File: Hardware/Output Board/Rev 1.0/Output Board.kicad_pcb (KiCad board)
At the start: 2 copper layers, 100 x 100 mm, 13 parts, among them J1 6502 Bus, J3 Conn_02x08_Odd_Even, U2 74HC138

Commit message: Working on Output Board
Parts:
- added C1: 100nF, Capacitor_SMD:C_0805_2012Metric, F.Cu at (109.5, 99.0)
- added C10: 100nF, Capacitor_SMD:C_0805_2012Metric, F.Cu at (130.8, 101.2)
- added C11: 4.7uF, Capacitor_SMD:C_0805_2012Metric, F.Cu at (130.8, 104.2)
- added C12: 4.7uF, Capacitor_SMD:C_0805_2012Metric, F.Cu at (130.8, 107.2)
- added C13: 100nF, Capacitor_SMD:C_0805_2012Metric, F.Cu at (99.6, 67.5)
- added C14: 100nF, Capacitor_SMD:C_0805_2012Metric, F.Cu at (131.8, 86.8)
- added C15: 2.7nF, Capacitor_SMD:C_0805_2012Metric, F.Cu at (111.2, 135.2)
- added C16: 100nF, Capacitor_SMD:C_0805_2012Metric, F.Cu at (105.8, 124.8)
- added C17: 100nF, Capacitor_SMD:C_0805_2012Metric, F.Cu at (157.8, 100.0)
- added C18: 100nF, Capacitor_SMD:C_0805_2012Metric, F.Cu at (162.2, 100.0)
- added C19: 100nF, Capacitor_SMD:C_0805_2012Metric, F.Cu at (157.8, 116.4)
- added C20: 1uF, Capacitor_SMD:C_0805_2012Metric, F.Cu at (115.7, 132.2)
- added C21: 2.7nF, Capacitor_SMD:C_0805_2012Metric, F.Cu at (115.7, 135.2)
- added C22: 2.2uF, Capacitor_SMD:C_0805_2012Metric, F.Cu at (120.2, 120.2)
- added C23: 1uF, Capacitor_SMD:C_0805_2012Metric, F.Cu at (120.2, 123.2)
- added C24: 4.7uF, Capacitor_SMD:C_0805_2012Metric, F.Cu at (120.2, 126.2)
- added C25: 4.7uF, Capacitor_SMD:C_0805_2012Metric, F.Cu at (120.2, 129.2)
- added C26: 10uF, Capacitor_SMD:C_0805_2012Metric, F.Cu at (125.2, 86.6)
- added C27: 10uF, Capacitor_SMD:C_0805_2012Metric, F.Cu at (113.7, 92.5)
- added C28: 10uF, Capacitor_SMD:C_0805_2012Metric, F.Cu at (141.6, 86.2)
- added C29: 10uF, Capacitor_SMD:C_0805_2012Metric, F.Cu at (146.3, 89.9)
- added C30: 100nF, Capacitor_SMD:C_0805_2012Metric, F.Cu at (173.2, 62.2)
- added C31: 100nF, Capacitor_SMD:C_0805_2012Metric, F.Cu at (158.3, 135.2)
- added C32: 100nF, Capacitor_SMD:C_0805_2012Metric, F.Cu at (161.9, 82.3)
- added C33: 100nF, Capacitor_SMD:C_0805_2012Metric, F.Cu at (180.3, 121.5)
- added C5: 100nF, Capacitor_SMD:C_0805_2012Metric, F.Cu at (126.3, 104.2)
- added C6: 100nF, Capacitor_SMD:C_0805_2012Metric, F.Cu at (126.3, 107.2)
- added C7: 4.7uF, Capacitor_SMD:C_0805_2012Metric, F.Cu at (126.3, 110.2)
- added C8: 4.7uF, Capacitor_SMD:C_0805_2012Metric, F.Cu at (126.3, 113.2)
- added C9: 100nF, Capacitor_SMD:C_0805_2012Metric, F.Cu at (126.3, 116.2)
- added J1: PROG, Connector_PinHeader_2.54mm:PinHeader_1x08_P2.54mm_Vertical, F.Cu at (97.7, 81.5)
- added J2: SD CARD, 6502 Parts:10067847-001RLF, F.Cu at (124.1, 55.7)
- added J3: AUDIO L, 6502 Parts:SWITCHCRAFT_PJRAN1X1U02X, F.Cu at (110.0, 145.7)
- added J4: AUDIO R, 6502 Parts:SWITCHCRAFT_PJRAN1X1U02X, F.Cu at (122.2, 145.8)
- added J5: VGA, Connector_Dsub:DSUB-15-HD_Socket_Horizontal_P2.29x1.90mm_EdgePinOffset3.03mm_Housed_MountingHolesOffset4.94mm, F.Cu at (154.6, 143.0)
- added JP1: FLASH EN, Connector_PinHeader_2.54mm:PinHeader_1x02_P2.54mm_Vertical, F.Cu at (98.0, 111.3)
- added JP2: SolderJumper_2_Open, Jumper:SolderJumper-2_P1.3mm_Open_RoundedPad1.0x1.5mm, F.Cu at (152.7, 130.9)
- added JP3: SolderJumper_2_Bridged, Jumper:SolderJumper-2_P1.3mm_Bridged_RoundedPad1.0x1.5mm, F.Cu at (166.8, 124.6)
- added L1: NRS4018T2R2MDGJ, Inductor_SMD:L_Bourns-SRN4018, F.Cu at (113.7, 87.4)
- added R1: 10k, Resistor_SMD:R_0805_2012Metric, F.Cu at (102.5, 87.3)
- added R10: 560, Resistor_SMD:R_0805_2012Metric, F.Cu at (113.4, 125.0)
- added R11: 536, Resistor_SMD:R_0805_2012Metric, F.Cu at (137.2, 122.1)
- added R12: 1070, Resistor_SMD:R_0805_2012Metric, F.Cu at (137.2, 125.0)
- added R13: 47k, Resistor_SMD:R_0805_2012Metric, F.Cu at (93.2, 128.8)
- added R14: 47k, Resistor_SMD:R_0805_2012Metric, F.Cu at (105.7, 127.6)
- added R15: 560, Resistor_SMD:R_0805_2012Metric, F.Cu at (111.1, 129.3)
- added R16: 2150, Resistor_SMD:R_0805_2012Metric, F.Cu at (137.2, 136.8)
- added R17: 4300, Resistor_SMD:R_0805_2012Metric, F.Cu at (141.6, 116.2)
- added R18: 536, Resistor_SMD:R_0805_2012Metric, F.Cu at (141.6, 119.2)
- added R19: 1070, Resistor_SMD:R_0805_2012Metric, F.Cu at (141.6, 122.1)
- added R2: 10k, Resistor_SMD:R_0805_2012Metric, F.Cu at (102.5, 90.2)
- added R20: 47k, Resistor_SMD:R_0805_2012Metric, F.Cu at (117.7, 91.6)
- added R21: 820, Resistor_SMD:R_0805_2012Metric, F.Cu at (141.6, 128.0)
- added R22: 2150, Resistor_SMD:R_0805_2012Metric, F.Cu at (141.6, 130.9)
- added R23: 47k, Resistor_SMD:R_0805_2012Metric, F.Cu at (121.4, 91.6)
- added R24: 820, Resistor_SMD:R_0805_2012Metric, F.Cu at (141.6, 136.8)
- added R25: 4300, Resistor_SMD:R_0805_2012Metric, F.Cu at (146.0, 116.2)
- added R26: 536, Resistor_SMD:R_0805_2012Metric, F.Cu at (146.0, 119.2)
- added R27: 1070, Resistor_SMD:R_0805_2012Metric, F.Cu at (146.0, 122.1)
- added R28: 2150, Resistor_SMD:R_0805_2012Metric, F.Cu at (146.0, 125.0)
- added R29: 4300, Resistor_SMD:R_0805_2012Metric, F.Cu at (146.0, 128.0)
- added R3: 10k, Resistor_SMD:R_0805_2012Metric, F.Cu at (102.5, 93.2)
- added R4: 47k, Resistor_SMD:R_0805_2012Metric, F.Cu at (100.9, 62.3)
- added R5: 47k, Resistor_SMD:R_0805_2012Metric, F.Cu at (95.6, 72.0)
- added R6: 47k, Resistor_SMD:R_0805_2012Metric, F.Cu at (105.7, 57.5)
- added R7: 47k, Resistor_SMD:R_0805_2012Metric, F.Cu at (95.7, 77.1)
- added R8: 47k, Resistor_SMD:R_0805_2012Metric, F.Cu at (105.8, 61.9)
- added R9: 47k, Resistor_SMD:R_0805_2012Metric, F.Cu at (95.3, 67.6)
- added U1: ICE40UP5K-SG48ITR50, Package_DFN_QFN:QFN-48-1EP_7x7mm_P0.5mm_EP5.3x5.3mm, F.Cu at (140.2, 100.1)
- added U10: 74HC138, Package_SO:SOIC-16_3.9x9.9mm_P1.27mm, F.Cu at (160.0, 126.4)
- added U11: 74HC138, Package_SO:SOIC-16_3.9x9.9mm_P1.27mm, F.Cu at (164.0, 74.2)
- added U3: SN74CBTD3861PWR, Package_SO:TSSOP-24_4.4x7.8mm_P0.65mm, F.Cu at (160.0, 110.0)
- added U4: 74CBTLV3126PW, Package_SO:TSSOP-14_4.4x5mm_P0.65mm, F.Cu at (102.2, 73.0)
- added U5: 74LVC4245APW, Package_SO:TSSOP-24_4.4x7.8mm_P0.65mm, F.Cu at (160.0, 93.5)
- added U6: WM8524CGEDT, Package_SO:TSSOP-16_4.4x5mm_P0.65mm, F.Cu at (126.9, 129.8)
- added U7: W25Q16JVSNIQ, Package_SO:SOIC-8_3.9x4.9mm_P1.27mm, F.Cu at (99.5, 128.2)
- added U8: AP3417CKTR-G1, Package_TO_SOT_SMD:SOT-23-5, F.Cu at (120.5, 87.0)
- added U9: MIC5504-3.3YM5, Package_TO_SOT_SMD:SOT-23-5, F.Cu at (141.9, 90.8)
- added X1: SG5032CAN_25.000000M-TJGA3, Oscillator:Oscillator_SMD_SeikoEpson_SG8002LB-4Pin_5.0x3.2mm, F.Cu at (132.4, 92.4)
- C2: value 100nF -> 4.7uF
- U2: value 74HC138 -> 74AHC00; footprint Package_SO:SOIC-16_3.9x9.9mm_P1.27mm -> Package_SO:SOIC-14_3.9x8.7mm_P1.27mm
- moved G*** 99.0 mm to (157.6, 55.9), turned to 180 degrees
- moved C2 67.7 mm to (105.8, 66.9)
- moved J6 56.0 mm to (152.8, 79.2), turned to 180 degrees
- moved C3 55.9 mm to (125.4, 100.5)
- moved C4 29.1 mm to (125.9, 98.0)
- moved U2 11.7 mm to (109.5, 108.8)
- moved REF** 0.20 mm to (174.0, 144.0)
- renumbered J3 to J6, J1 to J7
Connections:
- C2 pad 1: VCC -> 3V3
- C3 pad 1: GND -> 3V3
- C3 pad 2: VCC -> GND
- C4 pad 1: VCC -> 3V3
- J7 pad 30: /A4 -> A4
- U2 pad 1: A10 -> FPGA_CDONE
- U2 pad 10: /$9400 -> Net-(U2-Pad10)
- U2 pad 11: /$9000 -> SD_SEL
- U2 pad 12: /$8C00 -> FPGA_CDONE
- U2 pad 13: /$8800 -> Net-(U2-Pad10)
- U2 pad 14: /$8400 -> 3V3
- U2 pad 2: A11 -> FPGA_CDONE
- U2 pad 3: A12 -> Net-(U2-Pad3)
- U2 pad 4: A13 -> SPI_SEL
- U2 pad 5: A14 -> SPI_SEL
- U2 pad 6: A15 -> Net-(U2-Pad10)
- U2 pad 7: /$9C00 -> GND
- U2 pad 8: GND -> FLASH_SEL
- U2 pad 9: /$9800 -> Net-(U2-Pad3)

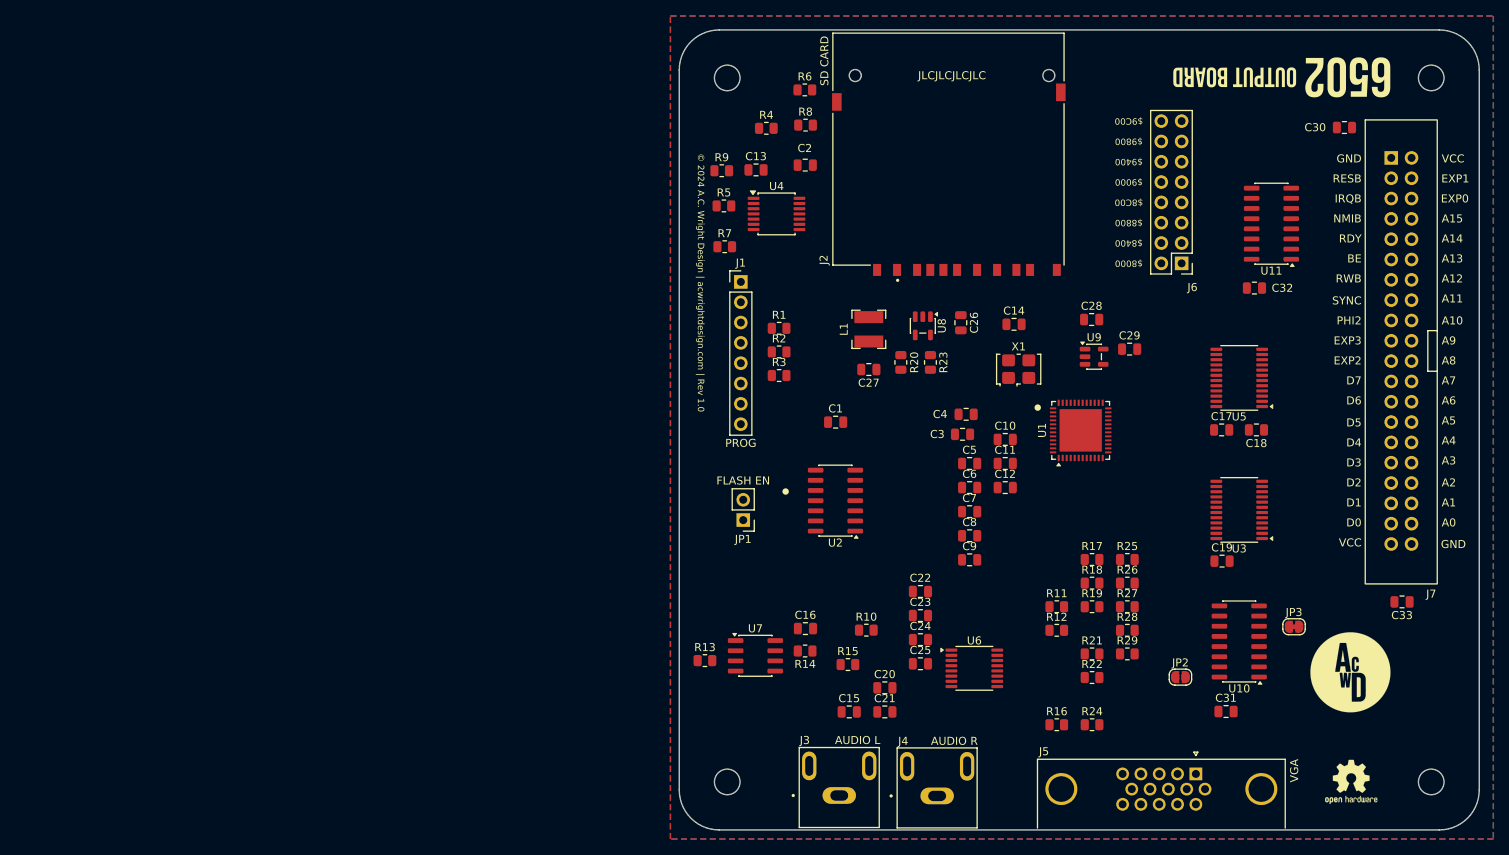
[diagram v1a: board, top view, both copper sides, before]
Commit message: Begin Output Board Redesign
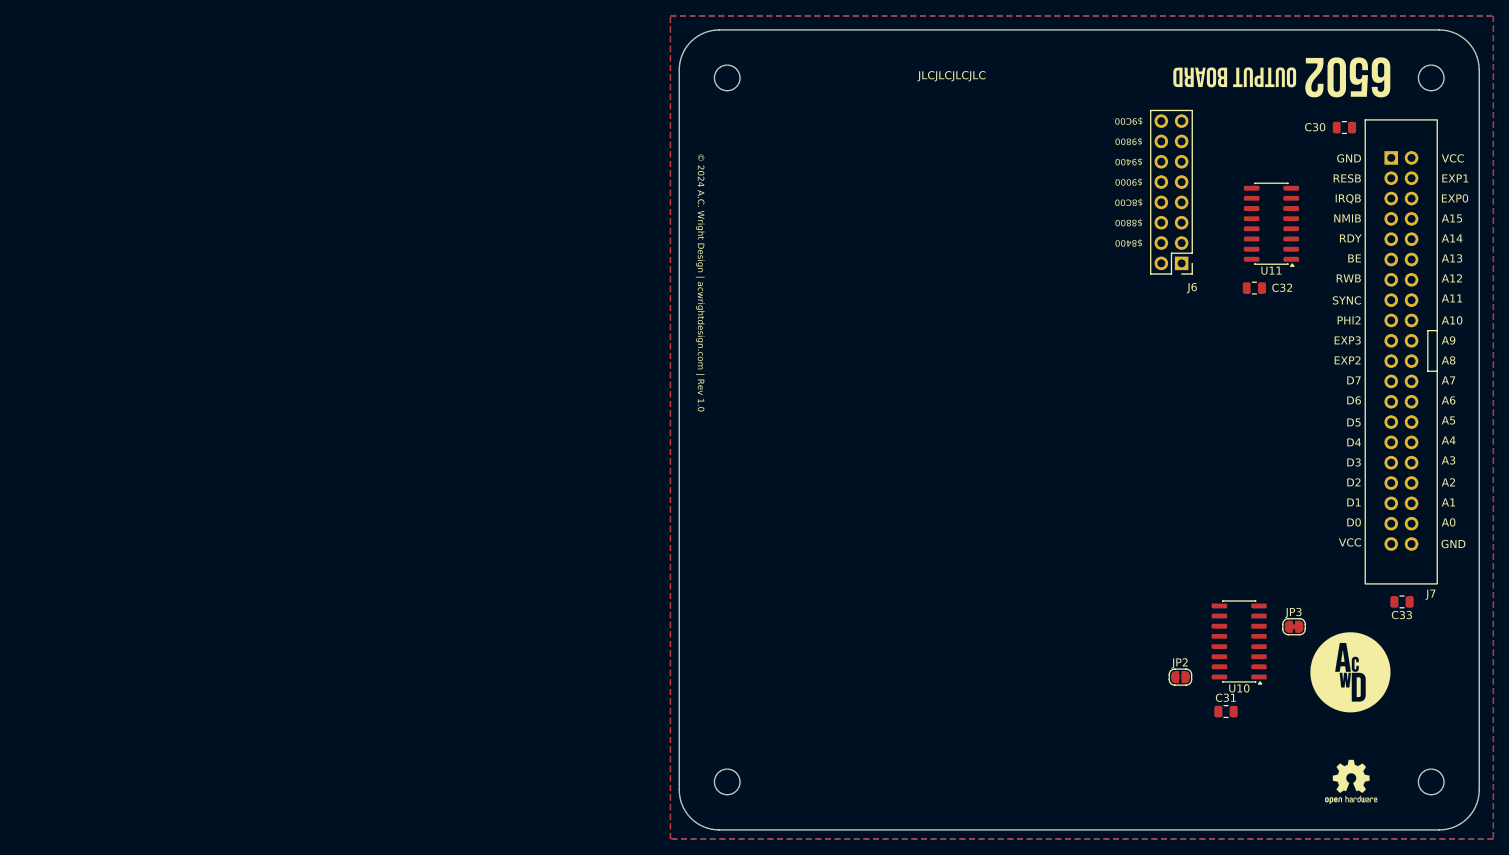
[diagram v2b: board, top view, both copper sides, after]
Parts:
- removed C1, C10, C13, C14, C16, C17, C18, C19, C3, C4, C5, C6, C9: 100nF, Capacitor_SMD:C_0805_2012Metric
- removed C11, C12, C2, C24, C25, C7, C8: 4.7uF, Capacitor_SMD:C_0805_2012Metric
- removed C15, C21: 2.7nF, Capacitor_SMD:C_0805_2012Metric
- removed C20, C23: 1uF, Capacitor_SMD:C_0805_2012Metric
- removed C22: 2.2uF, Capacitor_SMD:C_0805_2012Metric
- removed C26, C27, C28, C29: 10uF, Capacitor_SMD:C_0805_2012Metric
- removed J1: PROG, Connector_PinHeader_2.54mm:PinHeader_1x08_P2.54mm_Vertical
- removed J2: SD CARD, 6502 Parts:10067847-001RLF
- removed J3: AUDIO L, 6502 Parts:SWITCHCRAFT_PJRAN1X1U02X
- removed J4: AUDIO R, 6502 Parts:SWITCHCRAFT_PJRAN1X1U02X
- removed J5: VGA, Connector_Dsub:DSUB-15-HD_Socket_Horizontal_P2.29x1.90mm_EdgePinOffset3.03mm_Housed_MountingHolesOffset4.94mm
- removed JP1: FLASH EN, Connector_PinHeader_2.54mm:PinHeader_1x02_P2.54mm_Vertical
- removed L1: NRS4018T2R2MDGJ, Inductor_SMD:L_Bourns-SRN4018
- removed R1, R2, R3: 10k, Resistor_SMD:R_0805_2012Metric
- removed R10, R15: 560, Resistor_SMD:R_0805_2012Metric
- removed R11, R18, R26: 536, Resistor_SMD:R_0805_2012Metric
- removed R12, R19, R27: 1070, Resistor_SMD:R_0805_2012Metric
- removed R13, R14, R20, R23, R4, R5, R6, R7, R8, R9: 47k, Resistor_SMD:R_0805_2012Metric
- removed R16, R22, R28: 2150, Resistor_SMD:R_0805_2012Metric
- removed R17, R25, R29: 4300, Resistor_SMD:R_0805_2012Metric
- removed R21, R24: 820, Resistor_SMD:R_0805_2012Metric
- removed U1: ICE40UP5K-SG48ITR50, Package_DFN_QFN:QFN-48-1EP_7x7mm_P0.5mm_EP5.3x5.3mm
- removed U2: 74AHC00, Package_SO:SOIC-14_3.9x8.7mm_P1.27mm
- removed U3: SN74CBTD3861PWR, Package_SO:TSSOP-24_4.4x7.8mm_P0.65mm
- removed U4: 74CBTLV3126PW, Package_SO:TSSOP-14_4.4x5mm_P0.65mm
- removed U5: 74LVC4245APW, Package_SO:TSSOP-24_4.4x7.8mm_P0.65mm
- removed U6: WM8524CGEDT, Package_SO:TSSOP-16_4.4x5mm_P0.65mm
- removed U7: W25Q16JVSNIQ, Package_SO:SOIC-8_3.9x4.9mm_P1.27mm
- removed U8: AP3417CKTR-G1, Package_TO_SOT_SMD:SOT-23-5
- removed U9: MIC5504-3.3YM5, Package_TO_SOT_SMD:SOT-23-5
- removed X1: SG5032CAN_25.000000M-TJGA3, Oscillator:Oscillator_SMD_SeikoEpson_SG8002LB-4Pin_5.0x3.2mm
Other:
- board text removed: "$8000"

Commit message: Working on Output Board
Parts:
- removed C31: 100nF, Capacitor_SMD:C_0805_2012Metric
- added C1: 1uF, Capacitor_SMD:C_0805_2012Metric, F.Cu at (61.6, 89.2)
- added C10: 100nF, Capacitor_SMD:C_0805_2012Metric, F.Cu at (61.6, 107.3)
- added C2: 2.2nF, Capacitor_SMD:C_0805_2012Metric, F.Cu at (61.6, 92.2)
- added C3: 2.2nF, Capacitor_SMD:C_0805_2012Metric, F.Cu at (61.6, 95.2)
- added C4: 100nF, Capacitor_SMD:C_0805_2012Metric, F.Cu at (61.6, 98.3)
- added C7: 100nF, Capacitor_SMD:C_0805_2012Metric, F.Cu at (61.6, 101.3)
- added C9: 100nF, Capacitor_SMD:C_0805_2012Metric, F.Cu at (61.6, 104.3)
- added D1: D_Schottky, Diode_THT:D_DO-35_SOD27_P7.62mm_Horizontal, F.Cu at (65.4, 89.5)
- added FB1: BLM41PG600SN1L, Inductor_SMD:L_1806_4516Metric, F.Cu at (76.4, 100.8)
- added J1: VDD, Connector_JST:JST_XH_B2B-XH-A_1x02_P2.50mm_Vertical, F.Cu at (73.5, 120.9)
- added J2: AUDIO, 6502 Parts:SWITCHCRAFT_PJRAN1X1U02X, F.Cu at (65.8, 73.5)
- added J3: VIDEO, 6502 Parts:SWITCHCRAFT_PJRAN1X1U04X, F.Cu at (78.1, 73.5)
- added J4: INT Select, Connector_PinHeader_2.54mm:PinHeader_1x03_P2.54mm_Vertical, F.Cu at (64.4, 131.8)
- added JP1: SolderJumper_2_Bridged, Jumper:SolderJumper-2_P1.3mm_Bridged_RoundedPad1.0x1.5mm, F.Cu at (81.5, 104.3)
- added Q1: 2N4401, Package_TO_SOT_THT:TO-92_HandSolder, F.Cu at (74.8, 106.1)
- added R1: 1k, Resistor_SMD:R_0805_2012Metric, F.Cu at (70.6, 100.5)
- added R2: 470, Resistor_SMD:R_0805_2012Metric, F.Cu at (70.6, 103.5)
- added R3: 75, Resistor_SMD:R_0805_2012Metric, F.Cu at (70.6, 106.5)
- added U1: 6581, Socket:DIP_Socket-28_W11.9mm_W12.7mm_W15.24mm_W17.78mm_W18.5mm_3M_228-1277-00-0602J, F.Cu at (39.3, 90.6)
- added U2: Pico9918A, Socket:DIP_Socket-40_W11.9mm_W12.7mm_W15.24mm_W17.78mm_W18.5mm_3M_240-1280-00-0602J, F.Cu at (12.9, 90.6)
- renumbered C30 to C5, C33 to C6, C32 to C8, J6 to J5, J7 to J6, U10 to U3, U11 to U4
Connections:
- J5 pad 10: CSB -> CSBA
- J5 pad 12: CSB -> CSBV
- J5 pad 14: CSB -> CSBA
- J5 pad 16: CSB -> CSBV
- J5 pad 2: CSB -> CSBA
- J5 pad 4: CSB -> CSBV
- J5 pad 6: CSB -> CSBA
- J5 pad 8: CSB -> CSBV
- J6 pad 7: /NMIB -> NMIB
- U3 pad 2: CSB -> CSBV
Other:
- board text added: "$8000"

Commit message: Working on Output Board
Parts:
- added J3: VGA, Connector_FFC-FPC:Hirose_FH12-12S-0.5SH_1x12-1MP_P0.50mm_Horizontal, F.Cu at (121.7, 135.4)
- added J4: VGA, Connector_Dsub:DSUB-15-HD_Socket_Horizontal_P2.29x1.90mm_EdgePinOffset3.03mm_Housed_MountingHolesOffset4.94mm, F.Cu at (125.9, 142.6)
- moved U2 123.3 mm to (160.8, 112.0), turned to 180 degrees
- moved J2 120.1 mm to (161.8, 145.7)
- moved U1 117.8 mm to (128.6, 112.7), turned to 180 degrees
- moved J1 107.9 mm to (181.0, 130.3), turned to -90 degrees
- moved C2 106.9 mm to (167.0, 110.4), turned to -90 degrees
- moved C3 105.9 mm to (167.0, 105.3), turned to -90 degrees
- moved C1 105.6 mm to (157.1, 134.3)
- moved J5 101.8 mm to (149.8, 145.7)
- moved J6 100.0 mm to (135.6, 61.6), turned to 90 degrees
- moved R1 91.4 mm to (157.0, 130.5)
- moved C4 87.6 mm to (139.8, 137.8), turned to -90 degrees
- moved R3 84.1 mm to (150.0, 134.3)
- moved R2 83.8 mm to (149.9, 130.6)
- moved C9 77.3 mm to (138.9, 103.5), turned to 90 degrees
- moved Q1 74.0 mm to (143.4, 133.9)
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- renumbered J3 to J5, J4 to J6, J5 to J7, J6 to J8, U2 to U1, U1 to U2
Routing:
- net VCC: track 0.00 -> 55.8 mm, vias 0 -> 2
- net CSBV: track 0.00 -> 47.6 mm, vias 0 -> 4
- net Net-(J3-Pin_9): track 0.00 -> 23.5 mm, vias 0 -> 2
- net CSBA: track 0.00 -> 22.5 mm, vias 0 -> 4
- net Net-(JP2-B): track 0.00 -> 19.0 mm
- net Net-(J5-In): track 0.00 -> 18.8 mm
- net Net-(J3-Pin_11): track 0.00 -> 16.4 mm
- net Net-(J2-In): track 0.00 -> 15.2 mm
- net Net-(D1-A): track 0.00 -> 8.50 mm
- net INTB: track 0.00 -> 6.66 mm
- net Net-(U2-CAP2A): track 0.00 -> 6.49 mm, vias 0 -> 1
- net Net-(U2-CAP1A): track 0.00 -> 6.49 mm, vias 0 -> 1
- net Net-(J3-Pin_3): track 0.00 -> 6.37 mm
- net Net-(U2-CAP2B): track 0.00 -> 6.24 mm, vias 0 -> 1
- net Net-(U2-CAP1B): track 0.00 -> 6.22 mm, vias 0 -> 1
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
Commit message: Finish Output Board
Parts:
- removed C4: 100nF, Capacitor_SMD:C_0805_2012Metric
- removed FB1: BLM41PG600SN1L, Inductor_SMD:L_1806_4516Metric
- removed J3: VGA, Connector_FFC-FPC:Hirose_FH12-12S-0.5SH_1x12-1MP_P0.50mm_Horizontal
- removed J4: VGA, Connector_Dsub:DSUB-15-HD_Socket_Horizontal_P2.29x1.90mm_EdgePinOffset3.03mm_Housed_MountingHolesOffset4.94mm
- removed J5: VIDEO, 6502 Parts:SWITCHCRAFT_PJRAN1X1U04X
- removed Q1: 2N4401, Package_TO_SOT_THT:TO-92_HandSolder
- removed R2: 470, Resistor_SMD:R_0805_2012Metric
- removed R3: 75, Resistor_SMD:R_0805_2012Metric
- added REF**: MountingHole_3.2mm_M3, MountingHole:MountingHole_3.2mm_M3, F.Cu at (108.8, 138.0)
- added REF**: MountingHole_3.2mm_M3, MountingHole:MountingHole_3.2mm_M3, F.Cu at (133.8, 138.0)
- moved J2 8.52 mm to (153.2, 145.6)
- moved R1 8.52 mm to (148.5, 130.4)
- moved C1 8.52 mm to (148.6, 134.3)
- moved G*** 4.32 mm to (100.2, 127.8)
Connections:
- U1 pad 36: VIDEO -> unconnected-(U1-COMVID-Pad36)
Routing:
- net VCC: track 55.8 -> 214.2 mm, vias 2 -> 7
- net D4: track 0.00 -> 104.9 mm, vias 0 -> 6
- net RESB: track 0.00 -> 103.3 mm, vias 0 -> 4
- net PHI2: track 0.00 -> 103.1 mm, vias 0 -> 5
- net D5: track 0.00 -> 101.7 mm, vias 0 -> 8
- net RWB: track 0.00 -> 101.7 mm, vias 0 -> 3
- net D6: track 0.00 -> 96.3 mm, vias 0 -> 6
- net D0: track 0.00 -> 92.6 mm, vias 0 -> 4
- net D2: track 0.00 -> 92.3 mm, vias 0 -> 6
- net D3: track 0.00 -> 91.7 mm, vias 0 -> 4
- net D1: track 0.00 -> 91.4 mm, vias 0 -> 4
- net /$9800: track 0.00 -> 90.6 mm, vias 0 -> 3
- net D7: track 0.00 -> 90.4 mm, vias 0 -> 4
- net /$9400: track 0.00 -> 88.4 mm, vias 0 -> 3
- net /$9000: track 0.00 -> 86.2 mm, vias 0 -> 3
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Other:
- outline, holes or cut-outs redrawn
- board text added: "+"
- board text added: "-"
- board text added: "INTB"

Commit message: Production fixes
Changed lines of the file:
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@@
 		(sheetname "/")
 		(sheetfile "Output Board.kicad_sch")
-		(attr smd exclude_from_bom)
+		(attr smd)
 		(fp_line
 			(start -2.06 -5.06)
@@
 		(sheetname "/")
 		(sheetfile "Output Board.kicad_sch")
-		(attr through_hole)
+		(attr through_hole exclude_from_bom)
 		(fp_line
 			(start 19.17 39.94)
@@
 		)
 		(layer "Edge.Cuts")
-	)
-	(gr_line
-		(start 90.001101 145.0036)
-		(end 90.0011 145.0036)
-		(stroke
-			(width 0.05)
-			(type default)
-		)
-		(layer "Edge.Cuts")
